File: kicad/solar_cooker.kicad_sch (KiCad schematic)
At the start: 7 parts, among them U1 ATmega2560-16A, U2 microSD, U3 clock_module, U4 e-Paper, U5 anemometer

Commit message: schematic and documentation update
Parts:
- added U6: BME680, symbol custom_components:BME680
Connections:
- net A0: no longer U5.3 (SIG)
- net D4: now also R1.2, SW1.1 (A)
- net D5: no longer R1.2, SW1.1 (A)
- net GND: now also U6.2 (GND)
- net D6: now reaches U1.15 (PH3)
- net D6: now also U6.6 (CS)
- net D20 renamed SDA
- net SDA: no longer U1.44 (PD1)
- net D21 renamed SCL
- net SCL: no longer U1.43 (PD0)
- net D50 renamed MISO
- net MISO: now also U6.5 (SDO); no longer U1.22 (PB3)
- net D51 renamed MOSI
- net MOSI: now also U6.4 (SDA); no longer U1.21 (PB2)
- net D52 renamed SCK
- net SCK: now also U6.3 (SCL); no longer U1.20 (PB1)
- net VCC renamed +5V
- net +5V: now also U6.1 (VCC)
- new net A0 red: U5.3 (SIG)
- new net MISO/D50: U1.22 (PB3)
- new net MOSI/D51: U1.21 (PB2)
- new net SCK/D52: U1.20 (PB1)
- new net SCL/D21: U1.43 (PD0)
- new net SDA/D20: U1.44 (PD1)
- no-connect marks 58 -> 57
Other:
- moved on the sheet: U4, U5

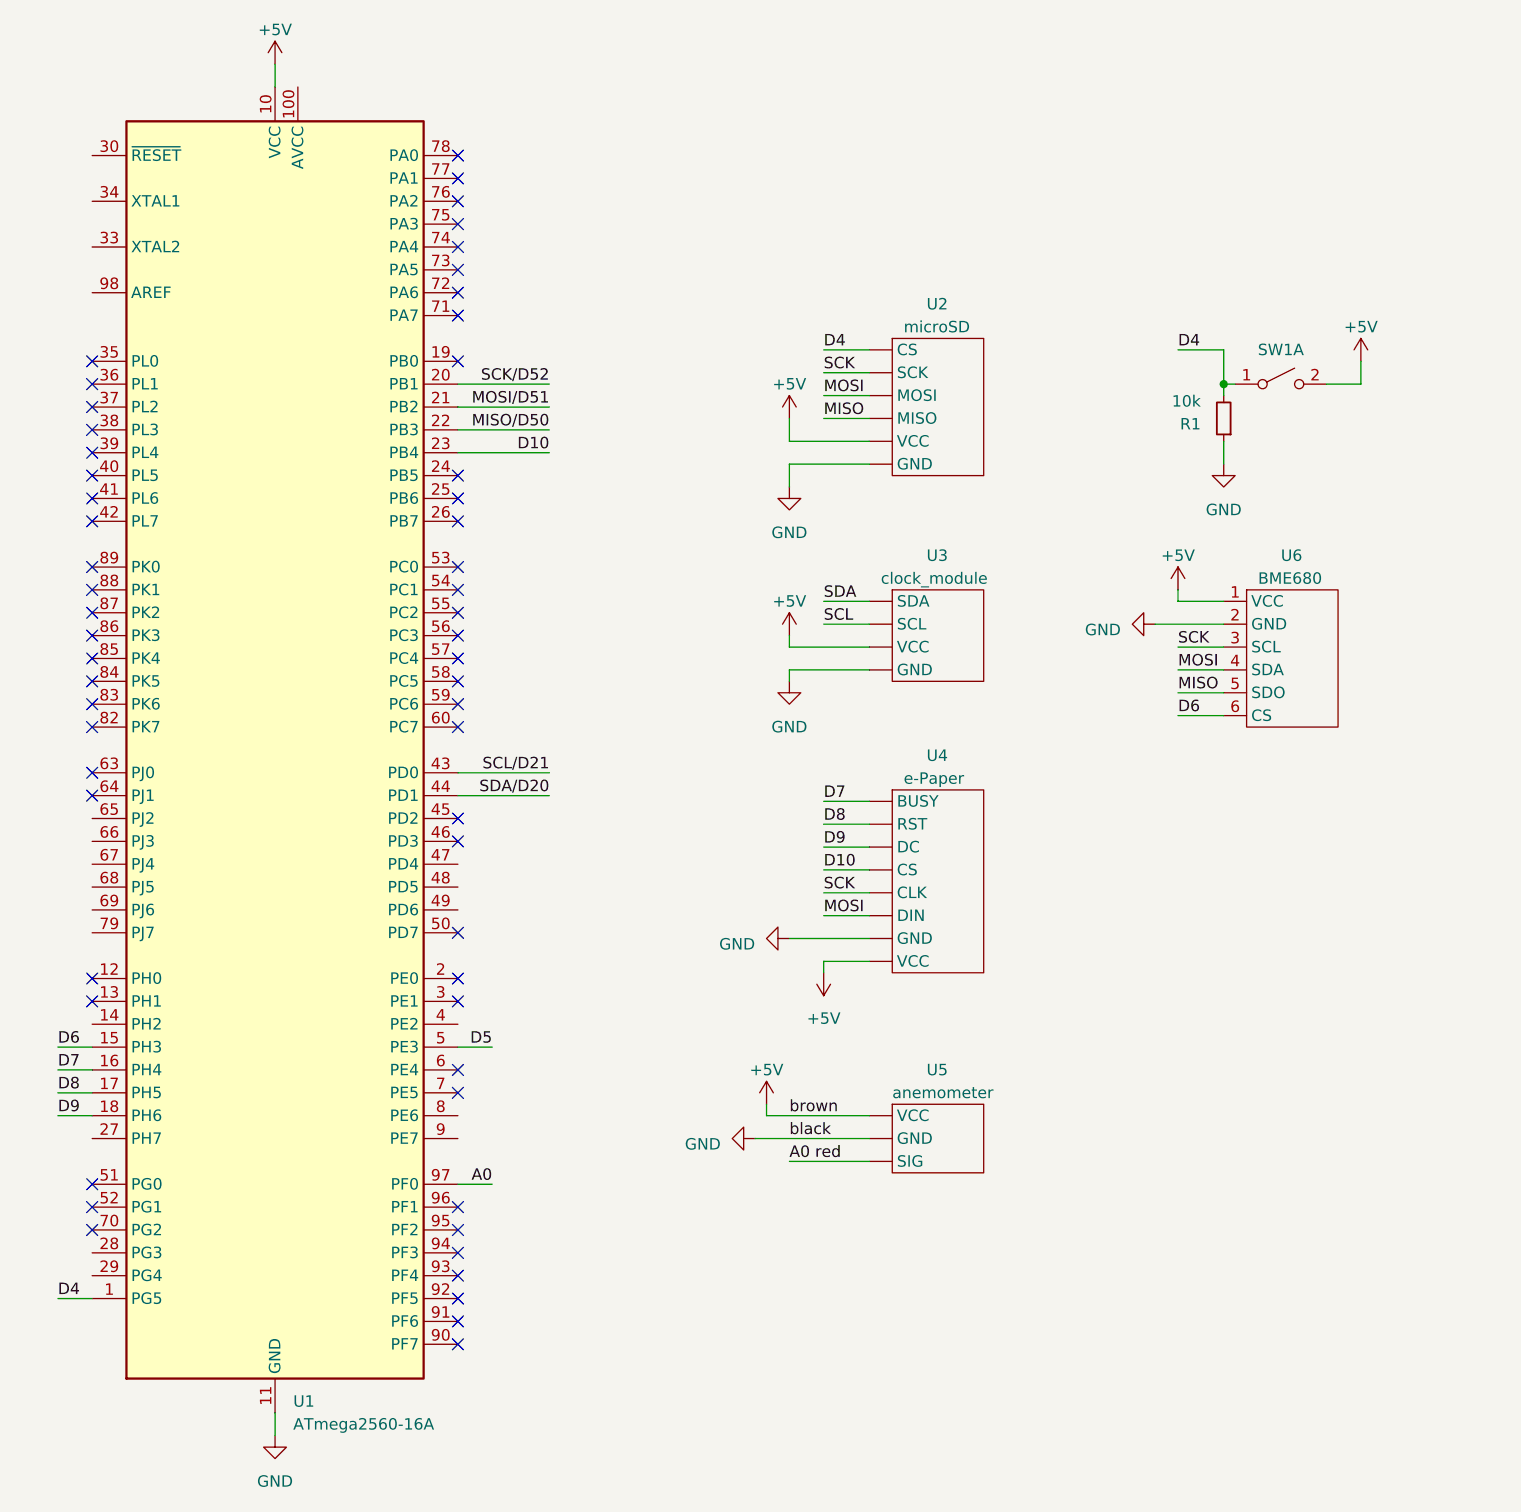
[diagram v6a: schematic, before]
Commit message: added PT100
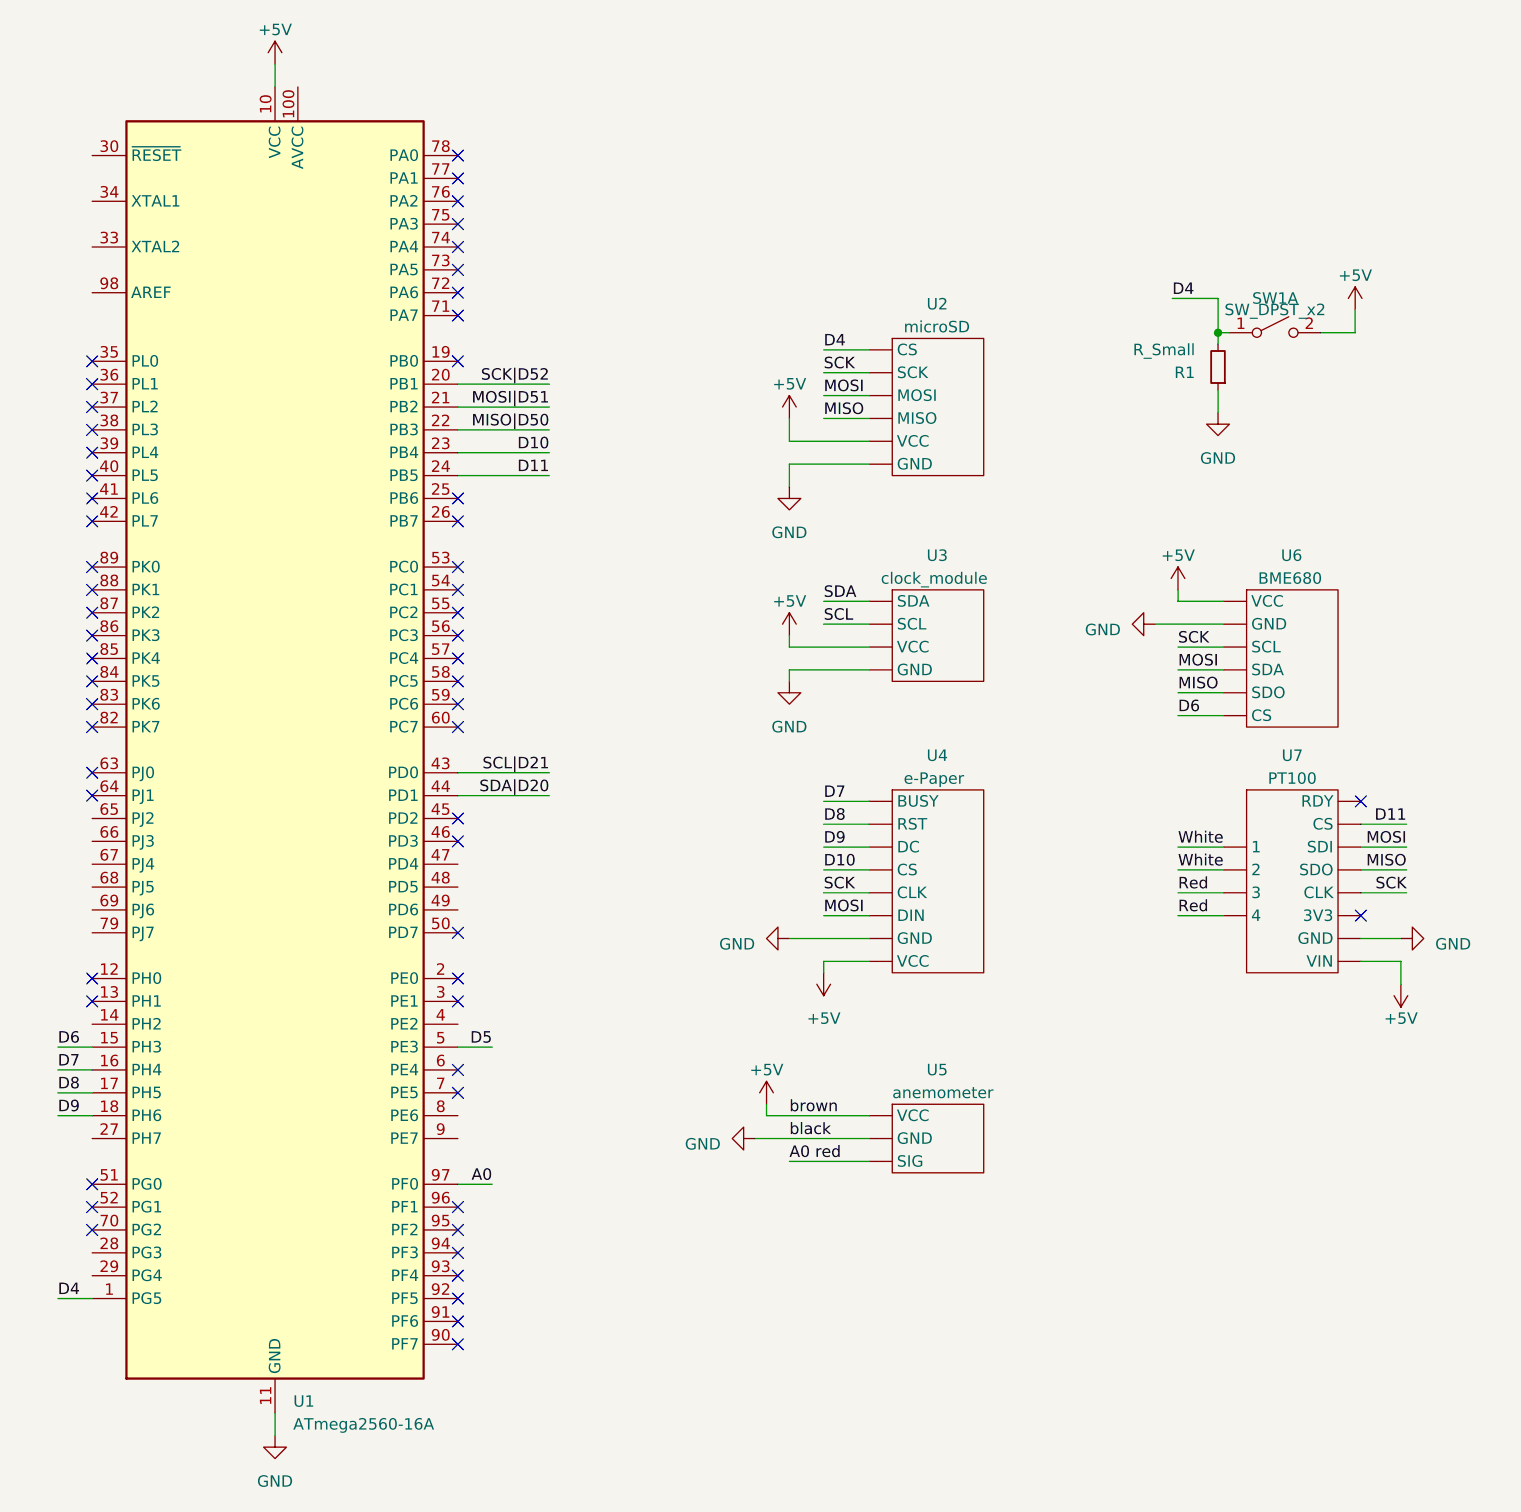
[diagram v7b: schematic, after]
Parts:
- added U7: PT100, symbol custom_components:temperature_inside_pot
- R1: value 10k -> R_Small
- SW1: value ~ -> SW_DPST_x2
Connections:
- net +5V: now also U7.12 (VIN)
- net GND: now also U7.11 (GND)
- net MISO: now also U7.8 (SDO)
- net MOSI: now also U7.7 (SDI)
- net SCK: now also U7.9 (CLK)
- net D11: now reaches U1.24 (PB5)
- net D11: now also U7.6 (CS)
- net MISO/D50 renamed MISO|D50
- net MOSI/D51 renamed MOSI|D51
- net SCK/D52 renamed SCK|D52
- net SCL/D21 renamed SCL|D21
- net SDA/D20 renamed SDA|D20
- new net Red: U7.3, U7.4
- new net White: U7.1, U7.2
- no-connect marks 57 -> 58
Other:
- moved on the sheet: R1, SW1A

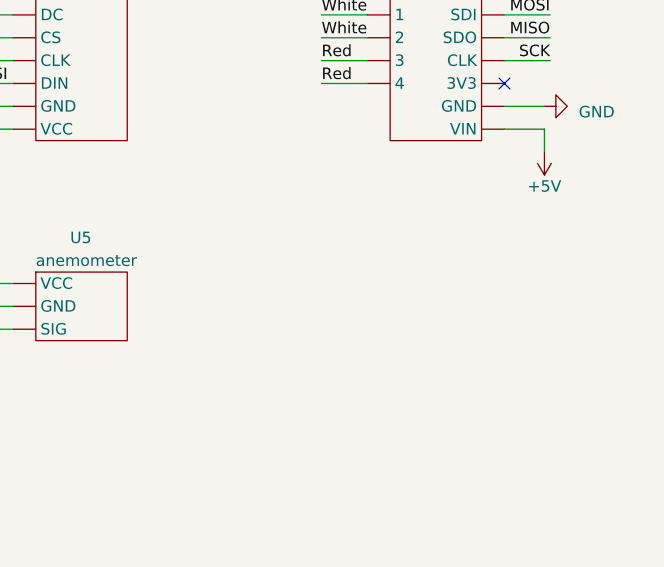
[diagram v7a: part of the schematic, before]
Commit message: added GPS schematic
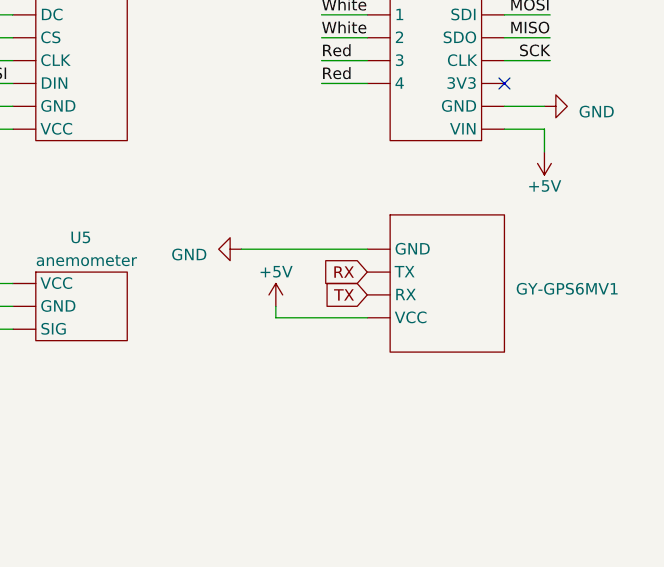
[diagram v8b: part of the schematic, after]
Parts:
- added GY-GPS6MV1: ~, symbol GPS:GY-GPS6MV2
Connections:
- net +5V: now also GY-GPS6MV1. (VCC)
- net GND: now also GY-GPS6MV1. (VCC)
- new net RX: GY-GPS6MV1. (VCC)
- new net TX: GY-GPS6MV1. (VCC)
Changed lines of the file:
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@@
     (stroke (width 0) (type default) (color 0 0 255 1))
+  )
+  (wire (pts (xy 160.02 142.24) (xy 170.18 142.24))
+    (stroke (width 0) (type default))
   )
   (wire (pts (xy 165.1 111.125) (xy 170.18 111.125))
@@
     (stroke (width 0) (type default) (color 0 0 255 1))
   )
+  (wire (pts (xy 156.21 134.62) (xy 170.18 134.62))
+    (stroke (width 0) (type default))
+  )
+  (wire (pts (xy 160.02 140.97) (xy 160.02 142.24))
+    (stroke (width 0) (type default))
+  )
   (wire (pts (xy 121.92 63.5) (xy 121.92 60.96))
     (stroke (width 0) (type default) (color 255 0 0 1))
@@
     (effects (font (size 1.27 1.27)) (justify left bottom))
   )
+  (global_label "TX" (shape input) (at 170.18 139.7 180) (fields_autoplaced)
+    (effects (font (size 1.27 1.27)) (justify right))
+    (property "Intersheetrefs" "${INTERSHEET_REFS}" (at 165.0971 139.7 0)
+      (effects (font (size 1.27 1.27)) (justify right) hide)
+    )
+  )
+  (global_label "RX" (shape input) (at 170.18 137.16 180) (fields_autoplaced)
+    (effects (font (size 1.27 1.27)) (justify right))
+    (property "Intersheetrefs" "${INTERSHEET_REFS}" (at 164.7947 137.16 0)
+      (effects (font (size 1.27 1.27)) (justify right) hide)
+    )
+  )
   (symbol (lib_id "power:GND") (at 121.92 118.745 270) (unit 1)
     (in_bom yes) (on_board yes) (dnp no) (fields_autoplaced)
@@
         (path "/61392a14-41f9-4325-aa01-94abd722c473"
           (reference "#PWR01") (unit 1)
+        )
+      )
+    )
+  )
+  (symbol (lib_id "GPS:GY-GPS6MV2") (at 179.07 138.43 0) (unit 1)
+    (in_bom yes) (on_board yes) (dnp no) (fields_autoplaced)
+    (property "Reference" "GY-GPS6MV1" (at 186.69 139.065 0)
+      (effects (font (size 1.27 1.27)) (justify left))
+    )
+    (property "Value" "~" (at 179.07 138.43 0)
+      (effects (font (size 1.27 1.27)))
+    )
+    (property "Footprint" "" (at 179.07 138.43 0)
+      (effects (font (size 1.27 1.27)) hide)
+    )
+    (property "Datasheet" "" (at 179.07 138.43 0)
+      (effects (font (size 1.27 1.27)) hide)
+    )
+    (pin "")
+    (pin "")
+    (pin "")
+    (pin "")
+    (instances
+      (project "solar_cooker"
+        (path "/61392a14-41f9-4325-aa01-94abd722c473"
+          (reference "GY-GPS6MV1") (unit 1)
         )
       )
@@
     )
   )
+  (symbol (lib_id "power:GND") (at 156.21 134.62 270) (unit 1)
+    (in_bom yes) (on_board yes) (dnp no) (fields_autoplaced)
+    (property "Reference" "#PWR018" (at 149.86 134.62 0)
+      (effects (font (size 1.27 1.27)) hide)
+    )
+    (property "Value" "GND" (at 152.4 135.255 90)
+      (effects (font (size 1.27 1.27)) (justify right))
+    )
+    (property "Footprint" "" (at 156.21 134.62 0)
+      (effects (font (size 1.27 1.27)) hide)
+    )
+    (property "Datasheet" "" (at 156.21 134.62 0)
+      (effects (font (size 1.27 1.27)) hide)
+    )
+    (pin "1")
+    (instances
+      (project "solar_cooker"
+        (path "/61392a14-41f9-4325-aa01-94abd722c473"
+          (reference "#PWR018") (unit 1)
+        )
+      )
+    )
+  )
   (symbol (lib_id "custom_components:microSD") (at 138.43 59.69 0) (unit 1)
     (in_bom yes) (on_board yes) (dnp no)
@@
         )
       )
+    )
+  )
+  (symbol (lib_id "power:+5V") (at 160.02 140.97 0) (unit 1)
+    (in_bom yes) (on_board yes) (dnp no) (fields_autoplaced)
+    (property "Reference" "#PWR017" (at 160.02 144.78 0)
+      (effects (font (size 1.27 1.27)) hide)
+    )
+    (property "Value" "+5V" (at 160.02 137.16 0)
+      (effects (font (size 1.27 1.27)))
+    )
+    (property "Footprint" "" (at 160.02 140.97 0)
+      (effects (font (size 1.27 1.27)) hide)
+    )
+    (property "Datasheet" "" (at 160.02 140.97 0)
+      (effects (font (size 1.27 1.27)) hide)
+    )
+    (pin "1")
+    (instances
+      (project "solar_cooker"
+        (path "/61392a14-41f9-4325-aa01-94abd722c473"
+          (reference "#PWR017") (unit 1)
+        )
+      )
